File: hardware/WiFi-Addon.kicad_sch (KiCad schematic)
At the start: 26 parts, among them J3 USB_B_Micro, U1 AMS1117-3.3, U2 ESP-12F, U3 CH340G

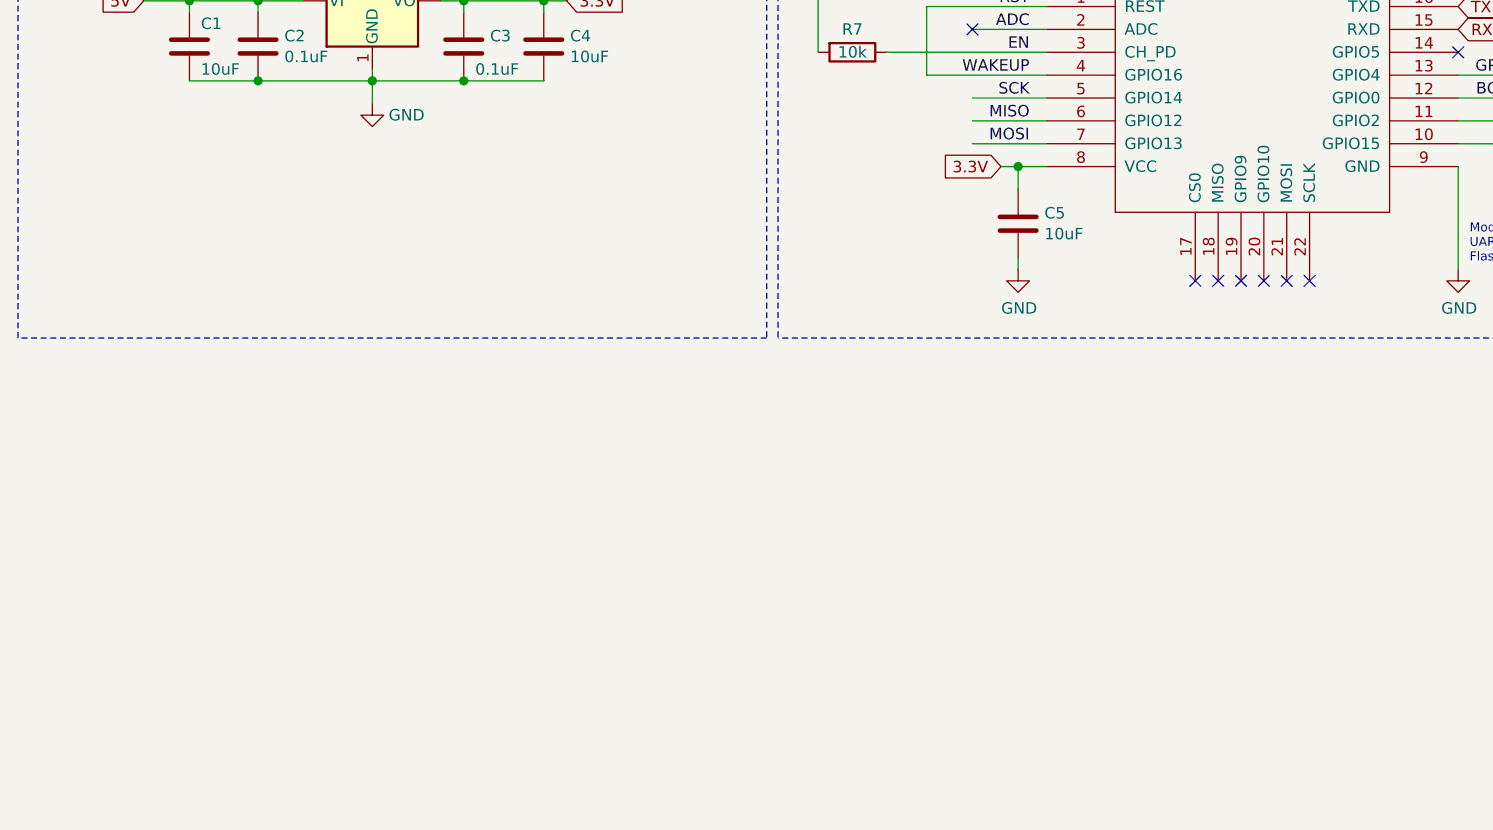
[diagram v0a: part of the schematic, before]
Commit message: Correcting footprint, and adding manufacturing markers
Gerber files & interactive BOM generated
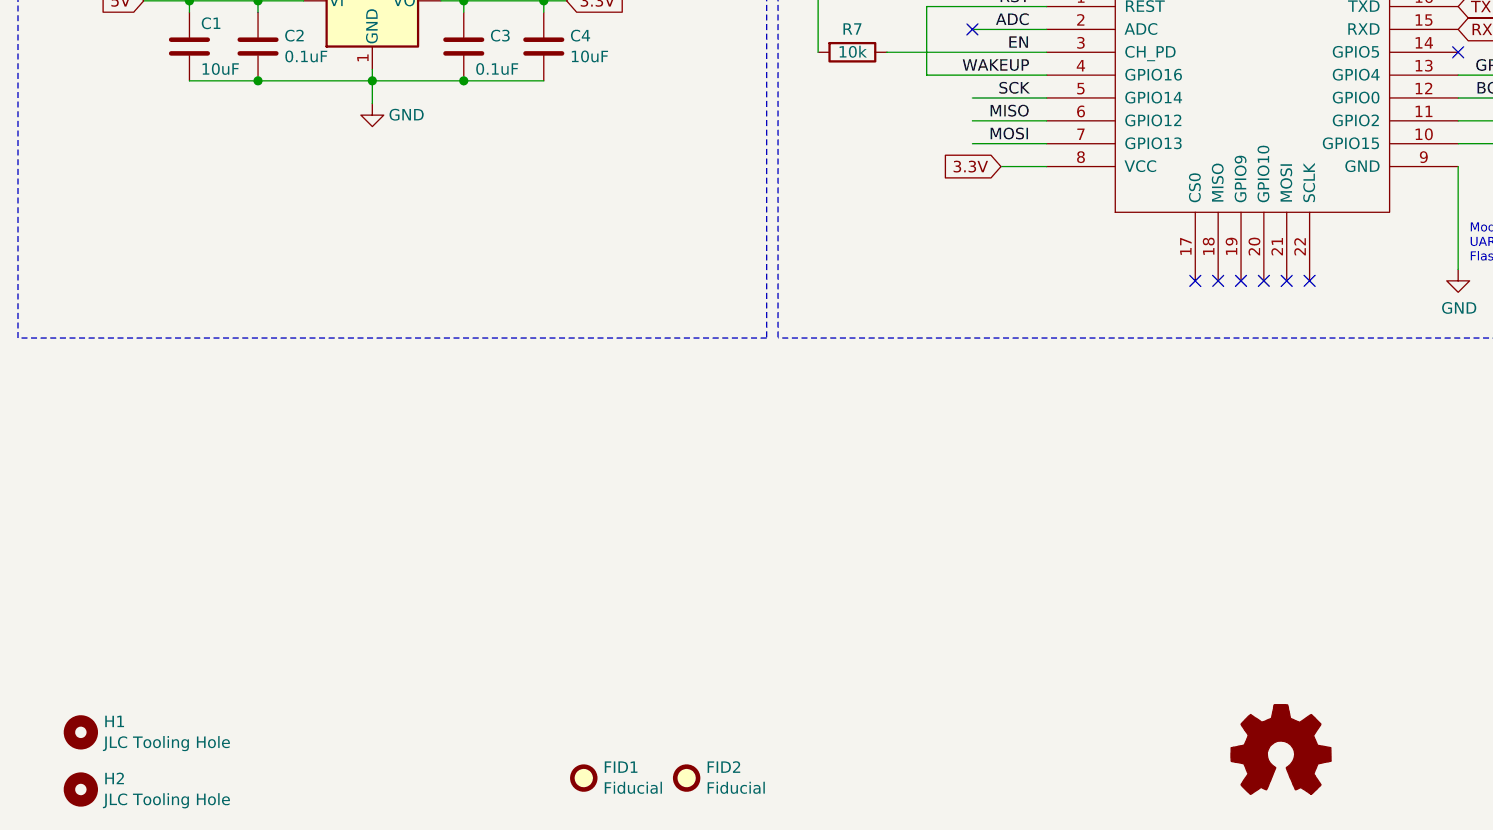
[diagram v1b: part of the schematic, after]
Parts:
- removed C5: 10uF, PrntrBoardV2:C_0603_1608Metric, symbol Device:C
- added FID1, FID2: Fiducial, PrntrBoardV2:Fiducial_1mm_Dia_2.54mm_Outer_CopperTop, symbol Mechanical:Fiducial
- added H1, H2: JLC Tooling Hole, PrntrBoardV2:JLC_Tool_hole, symbol Mechanical:MountingHole
- added LOGO1: Logo_Open_Hardware_Small, Symbol:OSHW-Logo2_9.8x8mm_SilkScreen, symbol Graphic:Logo_Open_Hardware_Small
- C6: LCSC Part # (none) -> C57112; Part # (none) -> 0603B103K500NT
- D1: LCSC Part # C8598 -> C8598
- R1, R4, R6: LCSC Part # (none) -> C23182; Part # (none) -> 0603WAF470JT5E
- R2: LCSC Part # (none) -> C23179; Part # (none) -> 0603WAF4700T5E
- R3, R5: LCSC Part # (none) -> C4190; Part # (none) -> 0603WAF2201T5E
- R7, R8: LCSC Part # (none) -> C25804; Part # (none) -> 0603WAF1002T5E
- U3: LCSC Part # (none) -> C99652; Part # (none) -> CH340E

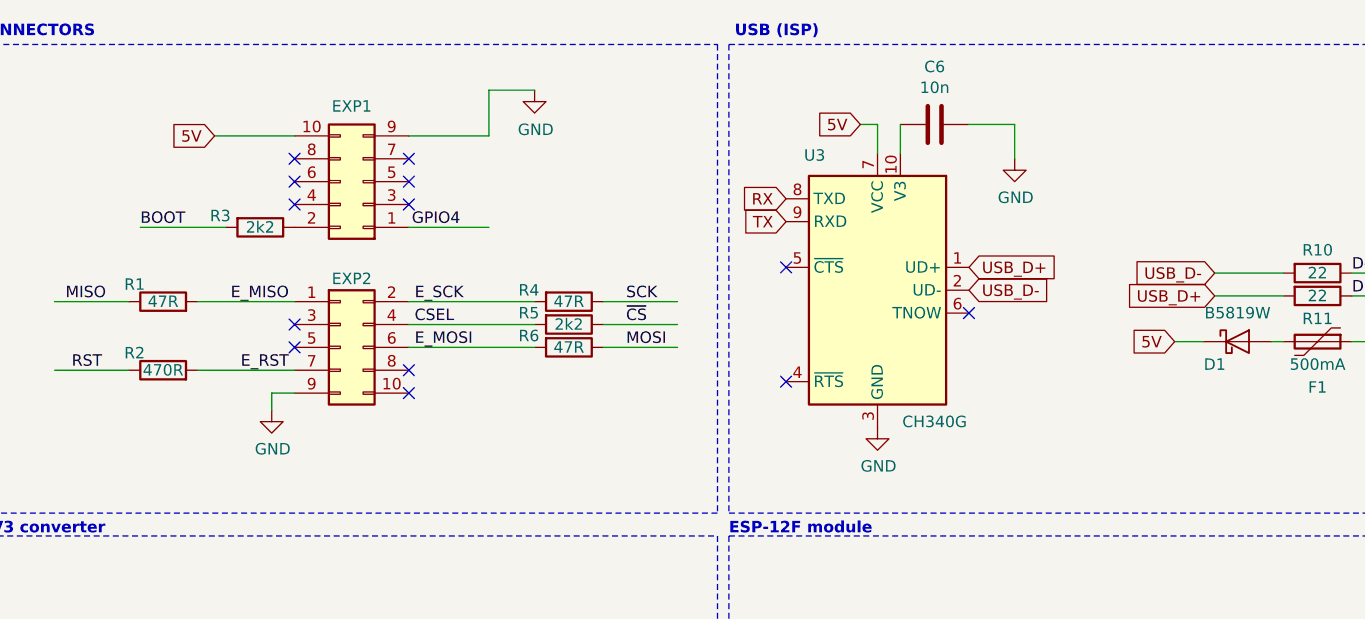
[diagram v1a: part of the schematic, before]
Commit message: Correction of header placement
Proper layer and spacing.
Plus small jumper to select USB or VIN power for WIFi
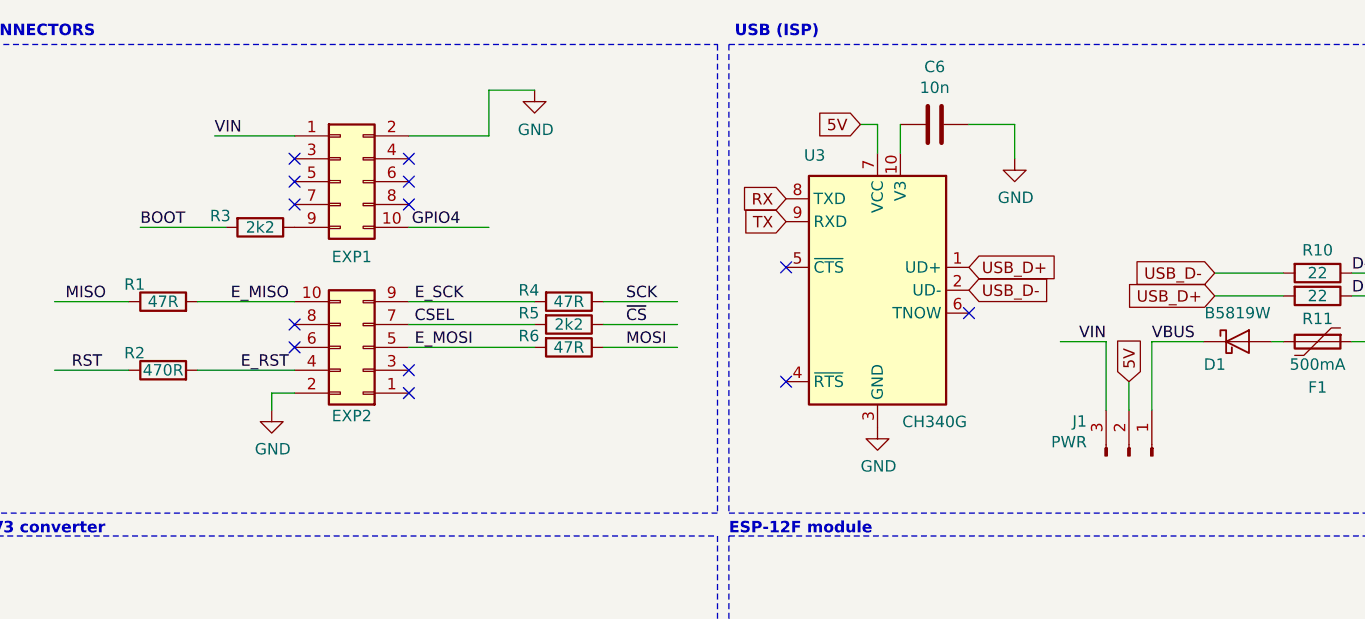
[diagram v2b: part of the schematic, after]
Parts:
- added J1: PWR, Connector_PinHeader_2.54mm:PinHeader_1x03_P2.54mm_Horizontal, symbol Connector:Conn_01x03_Male
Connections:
- net 5V: now also J1.2 (Pin_2); no longer D1.1 (K), EXP1.10 (Pin_10)
- net CSEL: now also EXP2.7 (Pin_7); no longer EXP2.4 (Pin_4)
- net E_MISO: now also EXP2.10 (Pin_10); no longer EXP2.1 (Pin_1)
- net E_MOSI: now also EXP2.5 (Pin_5); no longer EXP2.6 (Pin_6)
- net E_RST: now also EXP2.4 (Pin_4); no longer EXP2.7 (Pin_7)
- net E_SCK: now also EXP2.9 (Pin_9); no longer EXP2.2 (Pin_2)
- net GND: now also EXP1.2 (Pin_2), EXP2.2 (Pin_2); no longer EXP1.9 (Pin_9), EXP2.9 (Pin_9)
- net GPIO4: now also EXP1.10 (Pin_10); no longer EXP1.1 (Pin_1)
- net at R3.1: now also EXP1.9 (Pin_9); no longer EXP1.2 (Pin_2)
- new net VBUS: D1.1 (K), J1.1 (Pin_1)
- new net VIN: EXP1.1 (Pin_1), J1.3 (Pin_3)
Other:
- moved on the sheet: EXP1, EXP2
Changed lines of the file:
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@@
     (stroke (width 0) (type solid) (color 0 0 0 0))
   )
-  (wire (pts (xy 151.765 48.895) (xy 154.94 48.895))
+  (wire (pts (xy 144.145 48.895) (xy 139.065 48.895))
+    (stroke (width 0) (type solid) (color 0 0 0 0))
+  )
+  (wire (pts (xy 144.145 56.515) (xy 144.145 48.895))
+    (stroke (width 0) (type solid) (color 0 0 0 0))
+  )
+  (wire (pts (xy 146.685 53.34) (xy 146.685 56.515))
+    (stroke (width 0) (type solid) (color 0 0 0 0))
+  )
+  (wire (pts (xy 149.225 48.895) (xy 154.94 48.895))
+    (stroke (width 0) (type solid) (color 0 0 0 0))
+  )
+  (wire (pts (xy 149.225 56.515) (xy 149.225 48.895))
     (stroke (width 0) (type solid) (color 0 0 0 0))
   )
@@
     (effects (font (size 1.27 1.27)) (justify left bottom))
   )
+  (label "VIN" (at 45.085 26.035 0)
+    (effects (font (size 1.27 1.27)) (justify left bottom))
+  )
   (label "E_MISO" (at 53.34 44.45 180)
     (effects (font (size 1.27 1.27)) (justify right bottom))
@@
     (effects (font (size 1.27 1.27)) (justify right bottom))
   )
+  (label "VIN" (at 144.145 48.895 180)
+    (effects (font (size 1.27 1.27)) (justify right bottom))
+  )
+  (label "VBUS" (at 149.225 48.895 0)
+    (effects (font (size 1.27 1.27)) (justify left bottom))
+  )
   (label "D-" (at 171.45 41.275 0)
     (effects (font (size 1.27 1.27)) (justify left bottom))
@@
   )
   (global_label "5V" (shape input) (at 31.75 100.965 180)    (property "Intersheet References" "${INTERSHEET_REFS}" (id 0) (at -150.495 -14.605 0)
-      (effects (font (size 1.27 1.27)) hide)
-    )
-    (effects (font (size 1.27 1.27)) (justify right))
-  )
-  (global_label "5V" (shape input) (at 45.085 26.035 180)    (property "Intersheet References" "${INTERSHEET_REFS}" (id 0) (at -1.27 -80.645 0)
       (effects (font (size 1.27 1.27)) hide)
     )
@@
     (effects (font (size 1.27 1.27)) (justify left))
   )
-  (global_label "5V" (shape input) (at 151.765 48.895 180)    (property "Intersheet References" "${INTERSHEET_REFS}" (id 0) (at -30.48 -66.675 0)
-      (effects (font (size 1.27 1.27)) hide)
-    )
-    (effects (font (size 1.27 1.27)) (justify right))
+  (global_label "5V" (shape input) (at 146.685 53.34 90)    (property "Intersheet References" "${INTERSHEET_REFS}" (id 0) (at 262.255 -128.905 0)
+      (effects (font (size 1.27 1.27)) hide)
+    )
+    (effects (font (size 1.27 1.27)) (justify left))
   )
   (global_label "USB_D-" (shape input) (at 156.21 41.275 180)    (property "Intersheet References" "${INTERSHEET_REFS}" (id 0) (at -33.655 -66.675 0)
@@
     )
   )
+  (symbol (lib_id "Connector:Conn_01x03_Male") (at 146.685 61.595 270) (mirror x) (unit 1)
+    (in_bom yes) (on_board yes)
+    (property "Reference" "J1" (id 0) (at 142.0113 57.7532 90)
+      (effects (font (size 1.27 1.27)) (justify right))
+    )
+    (property "Value" "PWR" (id 1) (at 142.011 60.052 90)
+      (effects (font (size 1.27 1.27)) (justify right))
+    )
+    (property "Footprint" "Connector_PinHeader_2.54mm:PinHeader_1x03_P2.54mm_Horizontal" (id 2) (at 146.685 61.595 0)
+      (effects (font (size 1.27 1.27)) hide)
+    )
+    (property "Datasheet" "~" (id 3) (at 146.685 61.595 0)
+      (effects (font (size 1.27 1.27)) hide)
+    )
+  )
   (symbol (lib_id "Graphic:Logo_Open_Hardware_Small") (at 158.115 184.785 0) (unit 1)
     (in_bom no) (on_board yes)
@@
     )
   )
-  (symbol (lib_id "Connector_Generic:Conn_02x05_Odd_Even") (at 59.055 49.53 0) (unit 1)
-    (in_bom yes) (on_board yes)
-    (property "Reference" "EXP2" (id 0) (at 60.325 41.91 0))
-    (property "Value" "IDC 2x5" (id 1) (at 60.325 41.2496 0)
-      (effects (font (size 1.27 1.27)) hide)
-    )
-    (property "Footprint" "Connector_PinSocket_2.54mm:PinSocket_2x05_P2.54mm_Vertical" (id 2) (at 59.055 49.53 0)
-      (effects (font (size 1.27 1.27)) hide)
-    )
-    (property "Datasheet" "~" (id 3) (at 59.055 49.53 0)
-      (effects (font (size 1.27 1.27)) hide)
-    )
-    (property "Part #" "" (id 4) (at 59.055 49.53 0)
-      (effects (font (size 1.27 1.27)) hide)
-    )
-    (property "LCSC Part #" "C5661" (id 5) (at 59.055 49.53 0)
-      (effects (font (size 1.27 1.27)) hide)
-    )
-  )
-  (symbol (lib_id "Connector_Generic:Conn_02x05_Odd_Even") (at 61.595 31.115 180) (unit 1)
-    (in_bom yes) (on_board yes)
-    (property "Reference" "EXP1" (id 0) (at 60.325 22.752 0))
-    (property "Value" "IDC 2x5" (id 1) (at 60.325 39.3954 0)
-      (effects (font (size 1.27 1.27)) hide)
-    )
-    (property "Footprint" "Connector_PinSocket_2.54mm:PinSocket_2x05_P2.54mm_Vertical" (id 2) (at 61.595 31.115 0)
-      (effects (font (size 1.27 1.27)) hide)
-    )
-    (property "Datasheet" "~" (id 3) (at 61.595 31.115 0)
-      (effects (font (size 1.27 1.27)) hide)
-    )
-    (property "Part #" "" (id 4) (at 61.595 31.115 0)
-      (effects (font (size 1.27 1.27)) hide)
-    )
-    (property "LCSC Part #" "C5661" (id 5) (at 61.595 31.115 0)
+  (symbol (lib_id "Connector_Generic:Conn_02x05_Odd_Even") (at 59.055 31.115 0) (unit 1)
+    (in_bom yes) (on_board yes)
+    (property "Reference" "EXP1" (id 0) (at 60.325 39.478 0))
+    (property "Value" "IDC 2x5" (id 1) (at 60.325 22.8346 0)
+      (effects (font (size 1.27 1.27)) hide)
+    )
+    (property "Footprint" "Connector_PinSocket_2.54mm:PinSocket_2x05_P2.54mm_Vertical" (id 2) (at 59.055 31.115 0)
+      (effects (font (size 1.27 1.27)) hide)
+    )
+    (property "Datasheet" "~" (id 3) (at 59.055 31.115 0)
+      (effects (font (size 1.27 1.27)) hide)
+    )
+    (property "Part #" "" (id 4) (at 59.055 31.115 0)
+      (effects (font (size 1.27 1.27)) hide)
+    )
+    (property "LCSC Part #" "C5661" (id 5) (at 59.055 31.115 0)
+      (effects (font (size 1.27 1.27)) hide)
+    )
+  )
+  (symbol (lib_id "Connector_Generic:Conn_02x05_Odd_Even") (at 61.595 49.53 180) (unit 1)
+    (in_bom yes) (on_board yes)
+    (property "Reference" "EXP2" (id 0) (at 60.325 57.15 0))
+    (property "Value" "IDC 2x5" (id 1) (at 60.325 57.8104 0)
+      (effects (font (size 1.27 1.27)) hide)
+    )
+    (property "Footprint" "Connector_PinSocket_2.54mm:PinSocket_2x05_P2.54mm_Vertical" (id 2) (at 61.595 49.53 0)
+      (effects (font (size 1.27 1.27)) hide)
+    )
+    (property "Datasheet" "~" (id 3) (at 61.595 49.53 0)
+      (effects (font (size 1.27 1.27)) hide)
+    )
+    (property "Part #" "" (id 4) (at 61.595 49.53 0)
+      (effects (font (size 1.27 1.27)) hide)
+    )
+    (property "LCSC Part #" "C5661" (id 5) (at 61.595 49.53 0)
       (effects (font (size 1.27 1.27)) hide)
     )
@@
       (reference "H2") (unit 1) (value "JLC Tooling Hole") (footprint "PrntrBoardV2:JLC_Tool_hole")
     )
+    (path "/1a552ba4-8b78-49e6-b15c-99713fc317d2"
+      (reference "J1") (unit 1) (value "PWR") (footprint "Connector_PinHeader_2.54mm:PinHeader_1x03_P2.54mm_Horizontal")
+    )
     (path "/00000000-0000-0000-0000-00005daf169f"
